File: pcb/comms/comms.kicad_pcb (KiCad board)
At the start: 2 copper layers, 50 x 80 mm, 43 parts, among them IC1 STM32F437VIT6, IC2 ADP3335, IC3 MAX14787E, IC4 RJHSE-538x, J1 UART1, J2 UART2, J3 5v In, P1 USB-B, P2 SWD_TC, X5 Hole, X6 Hole, X8 Hole, X9 Hole, Y1 26M

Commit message: finished comms board
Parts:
- moved R3 196.1 mm to (39.7, 98.5), turned to 90 degrees
- moved C11 182.8 mm to (58.0, 96.8)
- moved R1 181.9 mm to (55.3, 93.7)
- moved C2 181.4 mm to (53.5, 91.8), turned to 270 degrees
- moved C15 180.1 mm to (46.6, 100.9)
- moved C8 180.1 mm to (58.0, 89.6)
- moved C7 180.1 mm to (58.0, 98.1)
- moved C1 179.2 mm to (57.7, 91.7), turned to 90 degrees
- moved C3 178.5 mm to (58.0, 88.3)
- moved C9 176.9 mm to (63.3, 102.8), turned to 90 degrees
- moved C6 173.8 mm to (62.3, 81.6), turned to 270 degrees
- moved C13 167.8 mm to (74.0, 102.9), turned to 270 degrees
- moved R7 166.9 mm to (37.0, 90.5), turned to 270 degrees
- moved C4 165.7 mm to (58.0, 95.5)
- moved TP1 165.6 mm to (85.1, 114.6), turned to 270 degrees
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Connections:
- C18 pad 1: 5v -> /OTG_HS_VBUS
- IC1 pad 1: Net-(IC1-Pad1) -> /LED2
- IC1 pad 2: Net-(IC1-Pad2) -> /LED1
- IC1 pad 45: /LED1 -> Net-(IC1-Pad45)
- IC1 pad 46: /LED2 -> Net-(IC1-Pad46)
- IC1 pad 51: Net-(IC1-Pad51) -> /STATUS
- IC1 pad 64: /STATUS -> Net-(IC1-Pad64)
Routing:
- net 5v: track 0.00 -> 80.7 mm, vias 0 -> 4
- net GND: track 0.00 -> 54.1 mm, vias 0 -> 87
- net 3v3: track 0.00 -> 48.9 mm, vias 0 -> 9
- net /~RST: track 0.00 -> 43.7 mm, vias 0 -> 2
- net /USART3_RX: track 0.00 -> 39.6 mm
- net /USART3_TX: track 0.00 -> 38.8 mm
- net /USART1_RX: track 0.00 -> 33.9 mm, vias 0 -> 1
- net /USART1_TX: track 0.00 -> 33.8 mm, vias 0 -> 1
- net /LED2: track 0.00 -> 26.3 mm
- net /LED1: track 0.00 -> 24.7 mm
- net /OTG_HS_VBUS: track 0.00 -> 22.6 mm, vias 0 -> 1
- net /RS485_TX: track 0.00 -> 19.6 mm, vias 0 -> 1
- net /OTG_HS_DP: track 0.00 -> 18.5 mm
- net /USART2_TX: track 0.00 -> 17.6 mm, vias 0 -> 1
- net /USART2_RX: track 0.00 -> 17.3 mm, vias 0 -> 1
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- added copper zone on In1.Cu, net 3v3
- added copper zone on B.Cu, net GND
- added copper zone on In2.Cu, net GND
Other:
- board size 50 x 80 mm -> 80 x 50 mm
- copper layers 2 -> 4
- net class Default: trace_width 0.25 -> 0.2
- rule via_min_drill: 0.3 -> 0.4
- rule via_min_size: 0.4 -> 0.6
- board text added: "+"
- board text added: "-"
- board text added: "11/11/18"
- board text added: "5v In"
- board text added: "A"
- board text added: "B"
- board text added: "BANK"
- board text added: "Communications Board"
- board text added: "Hybrid Ignition Controller"
- board text added: "Matt Coates"
- board text added: "RS485"
- board text added: "STATUS"

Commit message: pcbs complete
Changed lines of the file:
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@@
   )
   (setup
-    (last_trace_width 0.25)
+    (last_trace_width 0.2)
     (user_trace_width 0.2)
     (user_trace_width 0.25)
@@
       (net 7 GND))
   )
-  (gr_text "Hybrid Ignition Controller" (at 32 79) (layer F.SilkS)
+  (gr_text "Hybrid Ignition Controller" (at 32 75.75) (layer F.SilkS)
     (effects (font (size 2 2) (thickness 0.3) italic) (justify left))
   )
@@
     (effects (font (size 1.5 1.5) (thickness 0.3)))
   )
-  (gr_text "Communications Board" (at 32 76) (layer F.SilkS)
+  (gr_text "Communications Board" (at 32 79) (layer F.SilkS)
     (effects (font (size 2 2) (thickness 0.4)) (justify left))
   )

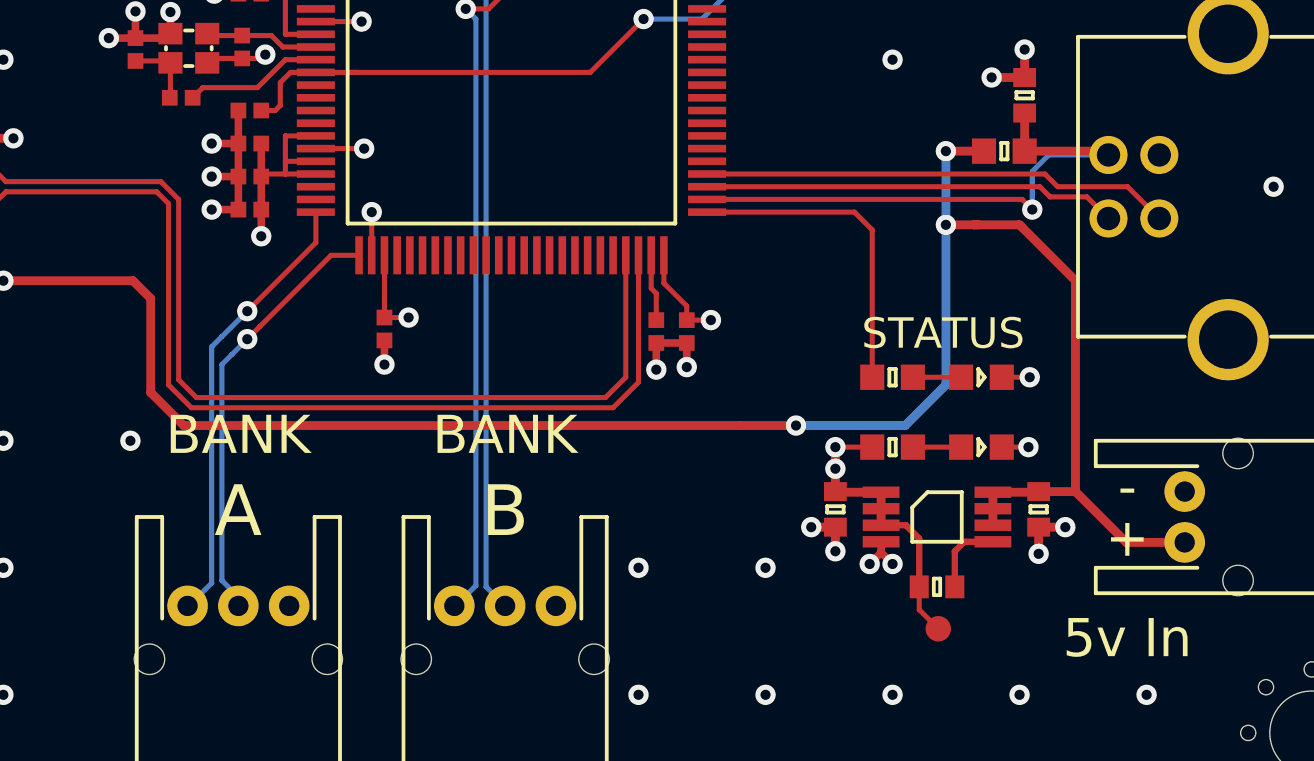
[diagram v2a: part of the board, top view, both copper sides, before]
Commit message: made changes to comms as per review
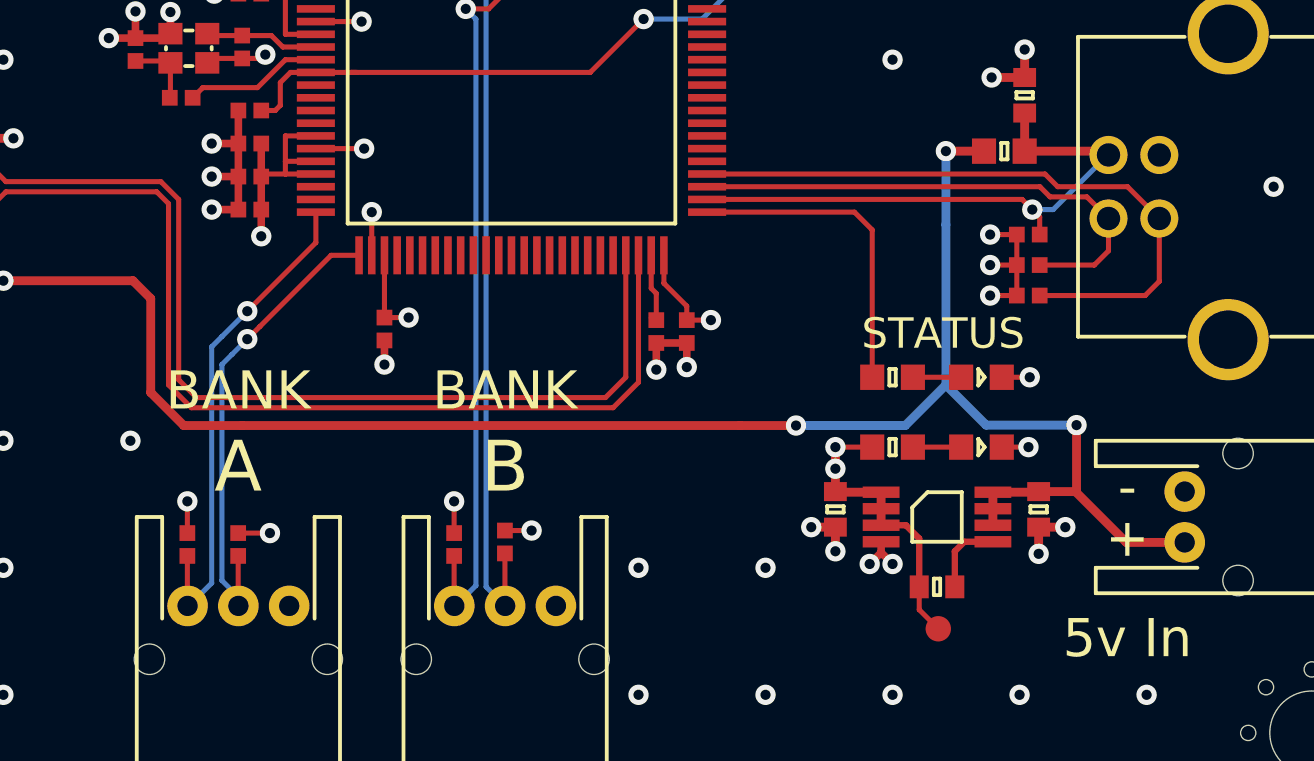
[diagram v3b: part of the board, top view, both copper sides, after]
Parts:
- added D3: ESD_DIODE, agg:0402, F.Cu at (88.6, 99.1)
- added D4: ESD_DIODE, agg:0402, F.Cu at (88.6, 101.5)
- added D5: ESD_DIODE, agg:0402, F.Cu at (88.6, 100.3)
- added D6: ESD_DIODE, agg:0402, F.Cu at (66.0, 111.3)
- added D7: ESD_DIODE, agg:0402, F.Cu at (68.0, 111.2)
- added D8: ESD_DIODE, agg:0402, F.Cu at (55.5, 111.3)
- added D9: ESD_DIODE, agg:0402, F.Cu at (57.5, 111.3)
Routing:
- net GND: track 54.1 -> 64.4 mm, vias 87 -> 94
- net /OTG_HS_DP: track 18.5 -> 25.9 mm
- net 5v: track 80.7 -> 74.2 mm
- net /OTG_HS_DM: track 16.3 -> 20.5 mm
- net /USART1_RX: track 33.9 -> 36.0 mm
- net /USART1_TX: track 33.8 -> 35.7 mm
- net /USART2_TX: track 17.6 -> 19.6 mm
- net /USART2_RX: track 17.3 -> 19.3 mm
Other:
- board text added: "Natalie's a babe."
